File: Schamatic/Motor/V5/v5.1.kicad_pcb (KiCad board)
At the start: 2 copper layers, 38.4 x 24 mm, 48 parts, among them J1 SWD, J10 GND, J11 V, J12 U, J13 W, J2 SPI, J3 RS485, J4 RS485, J5 CAP+, J6 12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

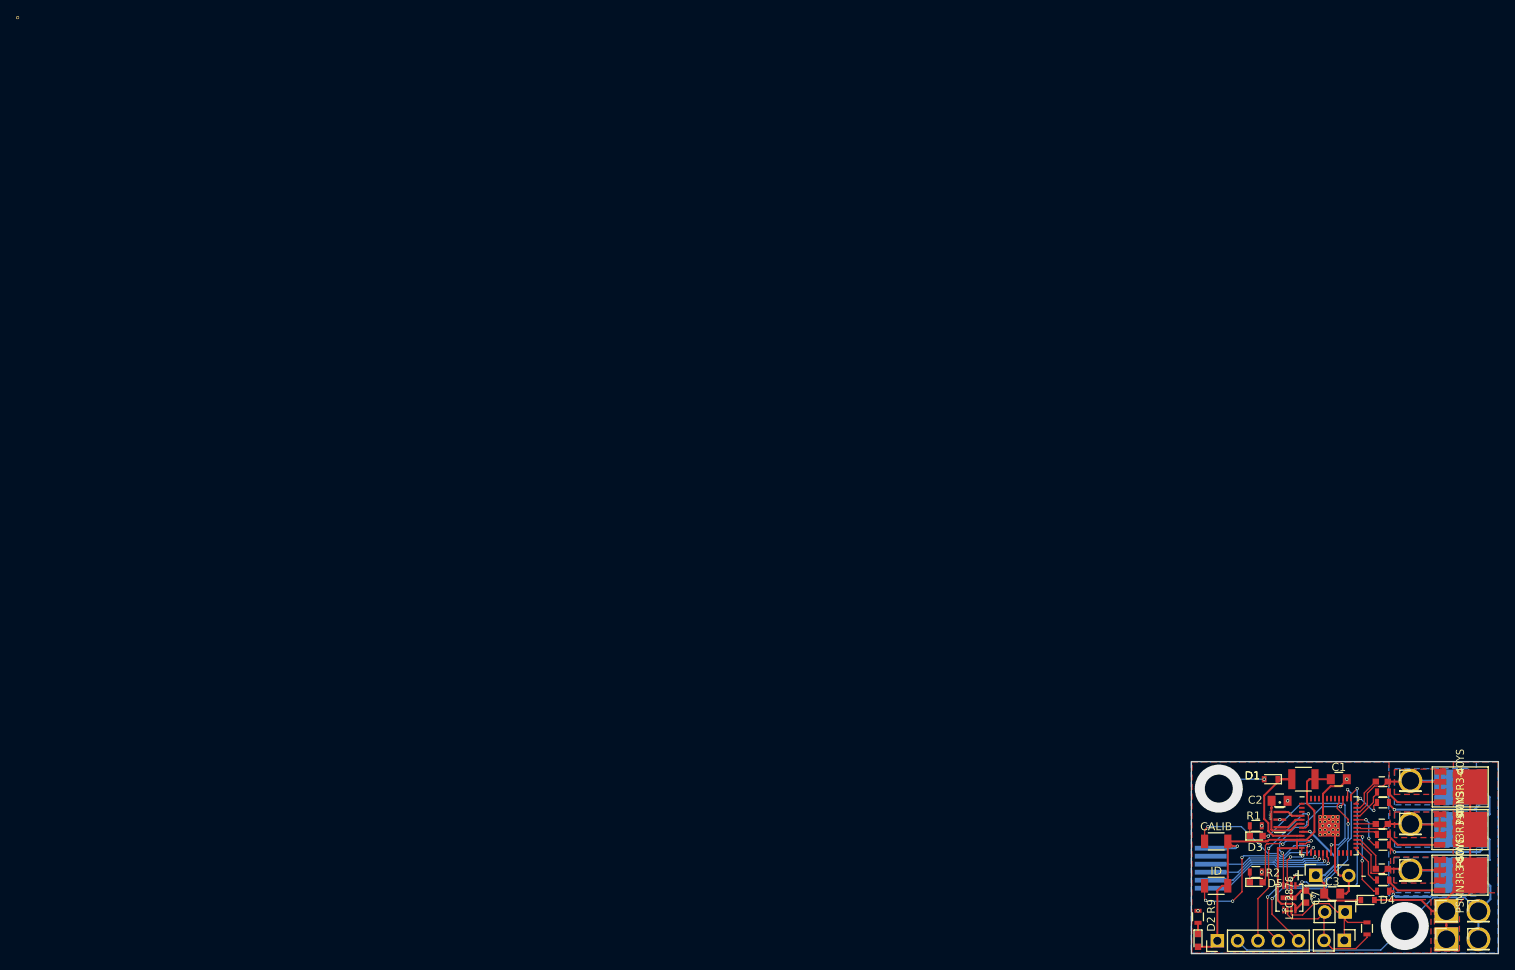
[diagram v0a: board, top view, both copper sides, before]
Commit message: motor PCB optimization
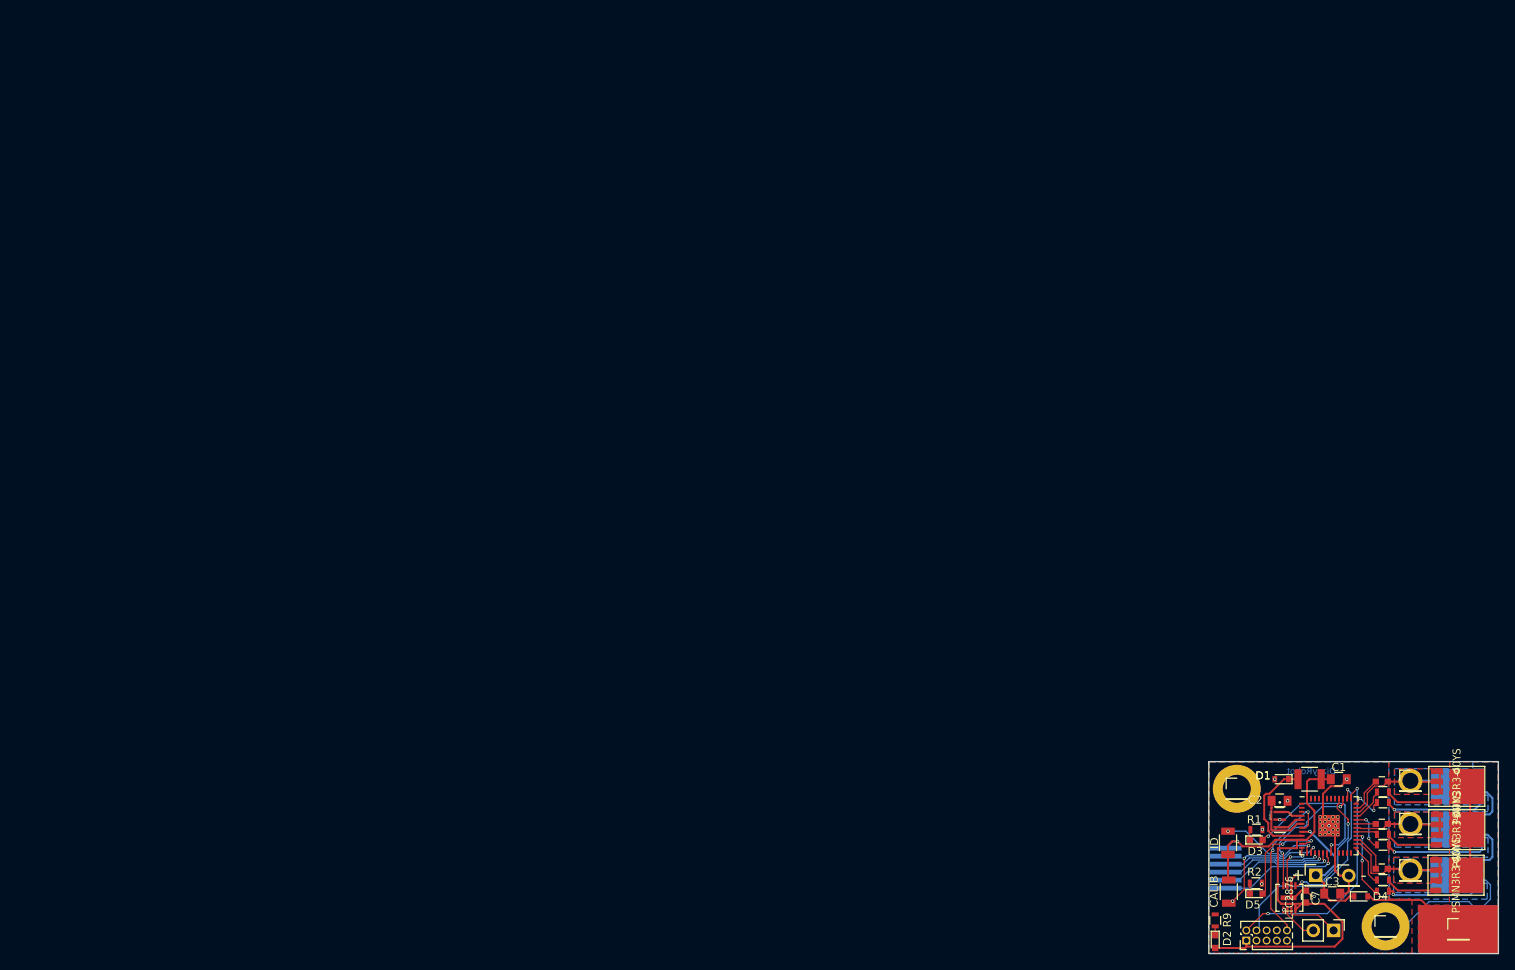
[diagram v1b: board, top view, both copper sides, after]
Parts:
- removed J10: GND, Pin_Headers:Pin_Header_Straight_1x01_Pitch2.54mm
- removed R10: 120, Resistors_SMD:R_0603
- removed REF**: VIA-0.4, VIA-0.4
- J1: value SWD -> CONN_02X05; footprint Pin_Headers:Pin_Header_Straight_1x05_Pitch2.54mm -> Pin_Headers:Pin_Header_Straight_2x05_Pitch1.27mm
- J4: value RS485 -> GND; footprint Pin_Headers:Pin_Header_Straight_1x02_Pitch2.54mm -> Pin_Headers:Pin_Header_Straight_1x01_Pitch2.54mm
- J7: value 12 -> GND
- J9: moved to B.Cu
- U1: footprint STSPIN32F0 -> Dizzy:STSPIN32F0
- moved J7 32.2 mm to (152.3, 96.4)
- moved CALIB 6.47 mm to (151.3, 109.2), turned to 90 degrees
- moved ID 5.57 mm to (151.2, 103.2), turned to 270 degrees
- moved J4 5.45 mm to (170.9, 113.6), turned to 0 degrees
- moved J1 3.63 mm to (153.5, 115.4)
- moved J9 2.84 mm to (179.9, 114.0)
- moved J3 2.71 mm to (164.4, 114.1)
- moved J6 2.70 mm to (180.0, 114.0)
- moved R9 2.20 mm to (149.6, 112.8)
- moved D2 2.16 mm to (149.6, 115.5)
- moved J2 1.85 mm to (153.9, 106.1)
- moved D5 1.40 mm to (154.7, 109.5)
- moved R2 1.40 mm to (154.7, 108.2)
- moved D1 1.33 mm to (157.9, 95.2)
- moved D4 0.96 mm to (167.8, 109.8)
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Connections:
- CALIB pad 1: Net-(SW1-Pad1) -> Net-(SW2-Pad1)
- ID pad 1: Net-(SW2-Pad1) -> Net-(SW1-Pad1)
- J1 pad 2: Earth -> SWDIO
- J1 pad 3: NRST -> Earth
- J1 pad 5: SWDIO -> Earth
- J4 pad 1: RS-B -> Earth
- J7 pad 1: +12V -> Earth
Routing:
- net Earth: track 91.8 -> 70.4 mm, vias 15 -> 12
- net +3V3: track 56.8 -> 70.6 mm
- net RS-A: track 16.2 -> 4.63 mm
- net RS-B: track 15.8 -> 6.67 mm
- net +12V: track 29.9 -> 21.7 mm
- net Net-(SW2-Pad1): track 21.7 -> 16.2 mm, vias 4 -> 3
- net Net-(SW1-Pad1): track 17.7 -> 12.9 mm
- net MOSI: track 17.6 -> 15.5 mm
- net MISO: track 16.5 -> 14.7 mm
- net SCK: track 15.3 -> 13.4 mm
- net CS: track 14.1 -> 12.3 mm
- net SWDIO: track 31.6 -> 29.7 mm
- net SWDCLK: track 28.6 -> 27.3 mm, vias 2 -> 1
- net Net-(D1-Pad1): track 15.1 -> 14.1 mm
- net NRST: track 21.2 -> 20.3 mm
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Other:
- board size 38.4 x 24 mm -> 36.2 x 24 mm
- board text added: "DizzyRobot"
- board text added: "SWD"
- board text removed: "IO"
- board text removed: "NRST"
- board text removed: "SWDCLK"

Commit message: minor corrections
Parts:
- moved J1 1.68 mm to (151.9, 114.9)
- moved J3 0.91 mm to (165.3, 114.0)
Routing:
- net +3V3: track 70.6 -> 72.9 mm
- net SWDIO: track 29.7 -> 31.1 mm
- net NRST: track 20.3 -> 19.2 mm
- net RS-B: track 6.67 -> 7.61 mm
- net RS-A: track 4.63 -> 5.57 mm
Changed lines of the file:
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@@
   (general
     (links 125)
-    (no_connects 1)
-    (area 148.749861 92.949999 185.050001 117.050001)
+    (no_connects 0)
+    (area 147.345 90.569999 185.13 122.058571)
     (thickness 1.6)
     (drawings 14)
-    (tracks 487)
+    (tracks 490)
     (zones 0)
     (modules 45)
@@
   )
   (module Pin_Headers:Pin_Header_Straight_1x02_Pitch2.54mm (layer F.Cu)
-    (at 164.4 114.1 270)
+    (at 165.3 114 270)
     (descr "Through hole straight pin header, 1x02, 2.54mm pitch, single row")
     (tags "Through hole pin header THT 1x02 2.54mm single row")
@@
   )
   (module Pin_Headers:Pin_Header_Straight_2x05_Pitch1.27mm (layer F.Cu)
-    (at 153.49 115.37 90)
+    (at 151.89 114.87 90)
     (descr "Through hole straight pin header, 2x05, 1.27mm pitch, double rows")
     (tags "Through hole pin header THT 2x05 1.27mm double row")
@@
   (gr_line (start 185 93) (end 185 117) (layer Edge.Cuts) (width 0.1))
   (gr_line (start 148.8 93) (end 185 93) (layer Edge.Cuts) (width 0.1))
+  (segment (start 157.86501 110.777594) (end 164.177594 110.777594) (width 0.25) (layer F.Cu) (net 1))
+  (segment (start 164.177594 110.777594) (end 166.4 113) (width 0.25) (layer F.Cu) (net 1))
+  (segment (start 166.4 113) (end 166.4 114.9) (width 0.25) (layer F.Cu) (net 1))
+  (segment (start 166.4 114.9) (end 165 116.3) (width 0.25) (layer F.Cu) (net 1))
+  (segment (start 165 116.3) (end 153.5 116.3) (width 0.25) (layer F.Cu) (net 1))
+  (segment (start 153.5 116.3) (end 151.8 116.3) (width 0.25) (layer F.Cu) (net 1))
+  (segment (start 149.6 116.3) (end 151.8 116.3) (width 0.25) (layer F.Cu) (net 1))
+  (segment (start 151.89 114.87) (end 151.89 115.62) (width 0.25) (layer F.Cu) (net 1))
+  (segment (start 151.89 115.62) (end 151.8 115.71) (width 0.25) (layer F.Cu) (net 1))
+  (segment (start 151.8 115.71) (end 151.8 116.3) (width 0.25) (layer F.Cu) (net 1))
   (segment (start 157.125 102.775) (end 159.825 102.775) (width 0.25) (layer F.Cu) (net 1))
   (segment (start 152.4 102.975) (end 153.025 103.6) (width 0.25) (layer F.Cu) (net 1))
   (segment (start 153.025 103.6) (end 156.3 103.6) (width 0.25) (layer F.Cu) (net 1))
   (segment (start 156.3 103.6) (end 157.125 102.775) (width 0.25) (layer F.Cu) (net 1))
-  (segment (start 153.495001 116.125001) (end 153.49 116.12) (width 0.25) (layer F.Cu) (net 1))
-  (segment (start 164.534001 116.125001) (end 153.495001 116.125001) (width 0.25) (layer F.Cu) (net 1))
-  (segment (start 165.505001 115.154001) (end 164.534001 116.125001) (width 0.25) (layer F.Cu) (net 1))
-  (segment (start 165.505001 113.045999) (end 165.505001 115.154001) (width 0.25) (layer F.Cu) (net 1))
-  (segment (start 163.236596 110.777594) (end 165.505001 113.045999) (width 0.25) (layer F.Cu) (net 1))
-  (segment (start 157.86501 110.777594) (end 163.236596 110.777594) (width 0.25) (layer F.Cu) (net 1))
   (segment (start 151.2 104.6) (end 151.2 103.5) (width 0.25) (layer F.Cu) (net 1))
   (segment (start 151.2 103.5) (end 151.725 102.975) (width 0.25) (layer F.Cu) (net 1))
   (segment (start 151.725 102.975) (end 152.4 102.975) (width 0.25) (layer F.Cu) (net 1))
-  (segment (start 153.49 116.12) (end 153.49 115.37) (width 0.25) (layer F.Cu) (net 1))
-  (segment (start 149.6 116.3) (end 153.31 116.3) (width 0.25) (layer F.Cu) (net 1))
-  (segment (start 153.31 116.3) (end 153.49 116.12) (width 0.25) (layer F.Cu) (net 1))
   (segment (start 151.2 104.6) (end 151.2 107.7) (width 0.25) (layer F.Cu) (net 1))
   (segment (start 151.2 107.7) (end 151.3 107.8) (width 0.25) (layer F.Cu) (net 1))
@@
   (segment (start 153.92857 108.2) (end 153.92857 109.49643) (width 0.13) (layer F.Cu) (net 17))
   (segment (start 153.92857 109.49643) (end 153.925 109.5) (width 0.13) (layer F.Cu) (net 17))
+  (segment (start 156.97 113.6) (end 156.97 112.892894) (width 0.13) (layer F.Cu) (net 18))
+  (segment (start 156.97 112.892894) (end 156.555597 112.478491) (width 0.13) (layer F.Cu) (net 18))
+  (segment (start 156.555597 112.478491) (end 156.555597 104.355595) (width 0.13) (layer F.Cu) (net 18))
+  (segment (start 156.555597 104.355595) (end 156.605597 104.305595) (width 0.13) (layer F.Cu) (net 18))
+  (segment (start 156.605597 104.305595) (end 156.805596 104.105596) (width 0.13) (layer F.Cu) (net 18))
   (segment (start 156.805596 103.411562) (end 156.805596 103.822754) (width 0.13) (layer B.Cu) (net 18))
-  (segment (start 156.555597 104.355595) (end 156.605597 104.305595) (width 0.13) (layer F.Cu) (net 18))
-  (segment (start 156.555597 111.378491) (end 156.555597 104.355595) (width 0.13) (layer F.Cu) (net 18))
-  (segment (start 158.57 114.1) (end 158.57 113.392894) (width 0.13) (layer F.Cu) (net 18))
-  (segment (start 156.605597 104.305595) (end 156.805596 104.105596) (width 0.13) (layer F.Cu) (net 18))
   (segment (start 160.917158 99.3) (end 156.805596 103.411562) (width 0.13) (layer B.Cu) (net 18))
   (segment (start 156.805596 103.822754) (end 156.805596 104.105596) (width 0.13) (layer B.Cu) (net 18))
-  (segment (start 158.57 113.392894) (end 156.555597 111.378491) (width 0.13) (layer F.Cu) (net 18))
   (via (at 156.805596 104.105596) (size 0.4) (drill 0.25) (layers F.Cu B.Cu) (net 18))
   (segment (start 161.2 99.3) (end 160.917158 99.3) (width 0.13) (layer B.Cu) (net 18))
@@
   (segment (start 161.25 100.93) (end 161.25 99.35) (width 0.13) (layer F.Cu) (net 18))
   (segment (start 161.25 99.35) (end 161.2 99.3) (width 0.13) (layer F.Cu) (net 18))
+  (segment (start 155.1 111.025) (end 155.1 111.66) (width 0.13) (layer B.Cu) (net 19))
+  (segment (start 155.1 111.66) (end 153.16 113.6) (width 0.13) (layer B.Cu) (net 19))
   (segment (start 166.15 96.5) (end 166.615011 96.965011) (width 0.13) (layer B.Cu) (net 19))
   (segment (start 166.615011 96.965011) (end 166.615011 102.54541) (width 0.13) (layer B.Cu) (net 19))
@@
   (segment (start 163.2077 108.635011) (end 161.191298 108.635011) (width 0.13) (layer B.Cu) (net 19))
   (segment (start 157.564989 108.560011) (end 155.1 111.025) (width 0.13) (layer B.Cu) (net 19))
-  (segment (start 155.1 113.76) (end 154.76 114.1) (width 0.13) (layer B.Cu) (net 19))
-  (segment (start 155.1 111.025) (end 155.1 113.76) (width 0.13) (layer B.Cu) (net 19))
   (segment (start 166.15 96.5) (end 166.15 97.55) (width 0.13) (layer F.Cu) (net 19))
   (segment (start 166.15 97.55) (end 166.075 97.625) (width 0.13) (layer F.Cu) (net 19))
   (via (at 166.15 96.5) (size 0.4) (drill 0.25) (layers F.Cu B.Cu) (net 19))
-  (segment (start 156.482842 112) (end 156.2 112) (width 0.13) (layer B.Cu) (net 20))
-  (segment (start 163.601002 112) (end 156.482842 112) (width 0.13) (layer B.Cu) (net 20))
+  (segment (start 156.443429 112) (end 156.160587 112) (width 0.13) (layer B.Cu) (net 20))
+  (segment (start 167.35 96.375) (end 167.35 108.251002) (width 0.13) (layer B.Cu) (net 20))
+  (segment (start 153.49 112) (end 155.877745 112) (width 0.13) (layer F.Cu) (net 20))
+  (segment (start 155.877745 112) (end 156.160587 112) (width 0.13) (layer F.Cu) (net 20))
+  (segment (start 163.601002 112) (end 156.443429 112) (width 0.13) (layer B.Cu) (net 20))
+  (via (at 156.160587 112) (size 0.4) (drill 0.25) (layers F.Cu B.Cu) (net 20))
+  (segment (start 151.89 113.6) (end 153.49 112) (width 0.13) (layer F.Cu) (net 20))
   (segment (start 167.35 108.251002) (end 163.601002 112) (width 0.13) (layer B.Cu) (net 20))
-  (segment (start 167.35 96.375) (end 167.35 108.251002) (width 0.13) (layer B.Cu) (net 20))
-  (segment (start 155.917158 112) (end 156.2 112) (width 0.13) (layer F.Cu) (net 20))
-  (segment (start 155.59 112) (end 155.917158 112) (width 0.13) (layer F.Cu) (net 20))
-  (segment (start 153.49 114.1) (end 155.59 112) (width 0.13) (layer F.Cu) (net 20))
-  (via (at 156.2 112) (size 0.4) (drill 0.25) (layers F.Cu B.Cu) (net 20))
   (segment (start 167.35 96.375) (end 166.575 97.15) (width 0.13) (layer F.Cu) (net 20))
   (segment (start 166.575 97.15) (end 166.575 97.625) (width 0.13) (layer F.Cu) (net 20))
@@
   (via (at 162.075 104.909968) (size 0.4) (drill 0.25) (layers F.Cu B.Cu) (net 24))
   (segment (start 162.075 104.425) (end 162.075 104.909968) (width 0.13) (layer F.Cu) (net 24))
+  (segment (start 164.4 114.1) (end 165.2 114.1) (width 0.13) (layer F.Cu) (net 25))
+  (segment (start 165.2 114.1) (end 165.3 114) (width 0.13) (layer F.Cu) (net 25))
   (segment (start 159.125 111.5363) (end 159.125 112.1108) (width 0.13) (layer F.Cu) (net 25))
   (segment (start 159.125 112.1108) (end 159.190001 112.175801) (width 0.13) (layer F.Cu) (net 25))
   (segment (start 159.190001 112.175801) (end 162.475801 112.175801) (width 0.13) (layer F.Cu) (net 25))
   (segment (start 162.475801 112.175801) (end 164.4 114.1) (width 0.13) (layer F.Cu) (net 25))
-  (segment (start 160.657919 114.1) (end 161.86 114.1) (width 0.13) (layer F.Cu) (net 26))
+  (segment (start 158.625 111.5363) (end 158.625 112.1108) (width 0.13) (layer F.Cu) (net 26))
   (segment (start 158.625 112.1108) (end 160.6142 114.1) (width 0.13) (layer F.Cu) (net 26))
-  (segment (start 158.625 111.5363) (end 158.625 112.1108) (width 0.13) (layer F.Cu) (net 26))
-  (segment (start 160.6142 114.1) (end 160.657919 114.1) (width 0.13) (layer F.Cu) (net 26))
+  (segment (start 160.6142 114.1) (end 162.66 114.1) (width 0.13) (layer F.Cu) (net 26))
+  (segment (start 162.66 114.1) (end 162.76 114) (width 0.13) (layer F.Cu) (net 26))
   (segment (start 171.322 96.8) (end 171.322 97) (width 0.25) (layer F.Cu) (net 27))
   (segment (start 171.322 97) (end 172.392 98.07) (width 0.25) (layer F.Cu) (net 27))

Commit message: BAU
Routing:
- net Net-(SW2-Pad1): vias 3 -> 2
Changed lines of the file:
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@@
     (thickness 1.6)
     (drawings 14)
-    (tracks 490)
+    (tracks 489)
     (zones 0)
     (modules 45)
@@
   (segment (start 151.775 110.45) (end 153.230014 108.994986) (width 0.13) (layer F.Cu) (net 40))
   (via (at 153.230014 105.1) (size 0.4) (drill 0.25) (layers F.Cu B.Cu) (net 40))
-  (via (at 151.775 110.45) (size 0.4) (drill 0.25) (layers F.Cu B.Cu) (net 40))
   (segment (start 161.575 104.425) (end 161.575 104.049814) (width 0.13) (layer F.Cu) (net 40))
   (segment (start 161.575 104.049814) (end 161.869963 103.754851) (width 0.13) (layer F.Cu) (net 40))
